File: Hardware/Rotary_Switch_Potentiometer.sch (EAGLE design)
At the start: 16 parts, among them SW1 1x10

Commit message: Small schem update.
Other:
- note added: "Resistor values can be selected for desired response."
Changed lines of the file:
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@@
 <text x="165.1" y="7.62" size="2.54" layer="94" font="vector">Byron Jacquot</text>
 <text x="238.76" y="7.62" size="2.54" layer="94" font="vector">V01</text>
+<text x="99.06" y="66.04" size="1.778" layer="97">Resistor values can be selected for desired response.</text>
 </plain>
 <instances>
@@
 </sheet>
 </sheets>
+<errors>
+</errors>
 </schematic>
 </drawing>

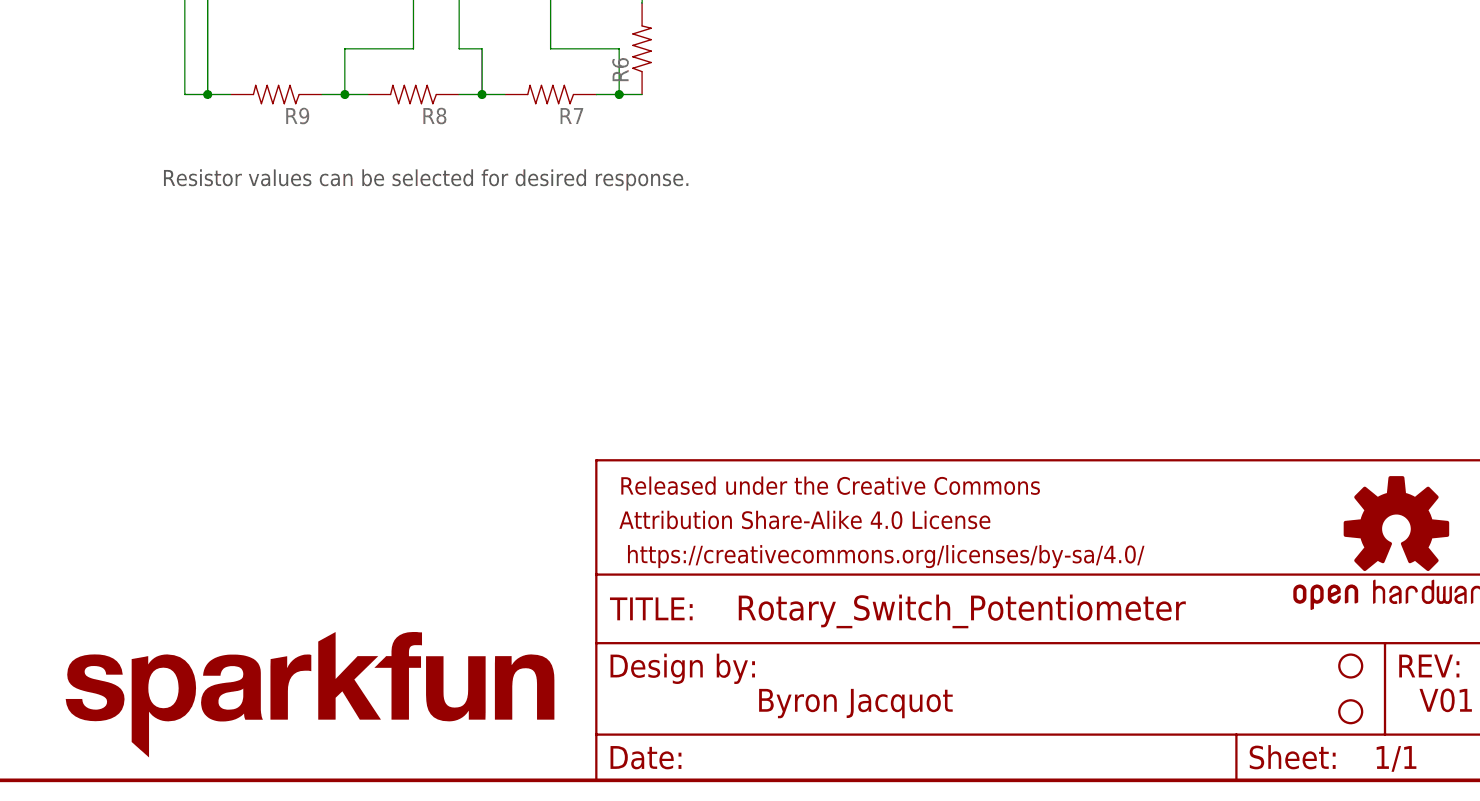
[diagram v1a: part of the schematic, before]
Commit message: Updates from working with protos.
Now has 4 mounting holes.
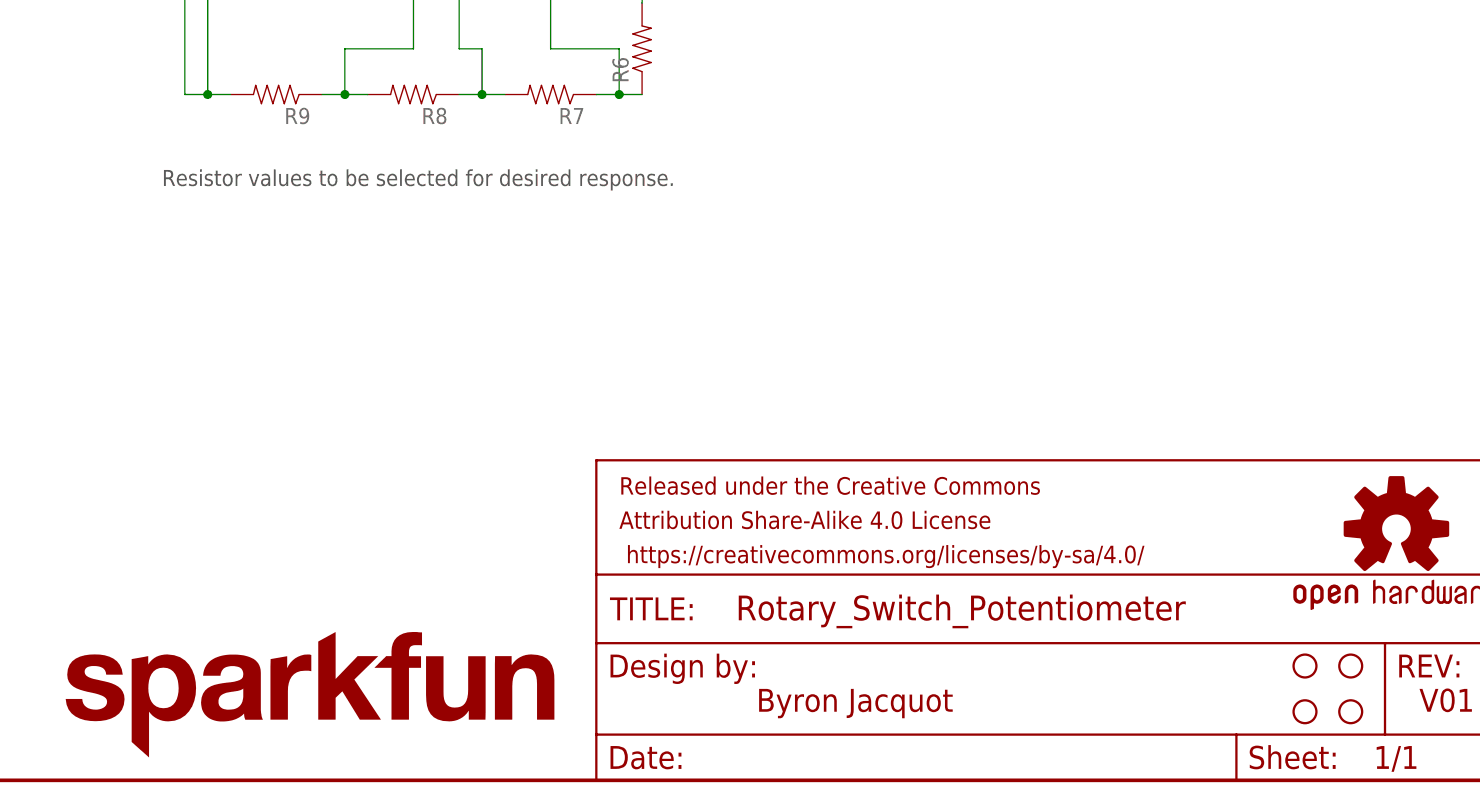
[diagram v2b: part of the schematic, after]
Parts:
- added STANDOFF5, STANDOFF6: STAND-OFF, SparkFun-Electromechanical:STAND-OFF
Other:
- note added: "Resistor values to be selected for desired response."
- note removed: "Resistor values can be selected for desired response."
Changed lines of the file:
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@@
 <?xml version="1.0" encoding="utf-8"?>
 <!DOCTYPE eagle SYSTEM "eagle.dtd">
-<eagle version="6.5.0">
+<eagle version="7.1.0">
 <drawing>
 <settings>
@@
 <part name="R8" library="SparkFun-Resistors" deviceset="RESISTOR" device="PTH-1/4W-VERT-KIT"/>
 <part name="R9" library="SparkFun-Resistors" deviceset="RESISTOR" device="PTH-1/4W-VERT-KIT"/>
+<part name="STANDOFF5" library="SparkFun-Electromechanical" deviceset="STAND-OFF" device=""/>
+<part name="STANDOFF6" library="SparkFun-Electromechanical" deviceset="STAND-OFF" device=""/>
 </parts>
 <sheets>
@@
 <text x="165.1" y="7.62" size="2.54" layer="94" font="vector">Byron Jacquot</text>
 <text x="238.76" y="7.62" size="2.54" layer="94" font="vector">V01</text>
-<text x="99.06" y="66.04" size="1.778" layer="97">Resistor values can be selected for desired response.</text>
+<text x="99.06" y="66.04" size="1.778" layer="97">Resistor values to be selected for desired response.</text>
 </plain>
 <instances>
@@
 <instance part="R8" gate="G$1" x="127" y="76.2" rot="R180"/>
 <instance part="R9" gate="G$1" x="111.76" y="76.2" rot="R180"/>
+<instance part="STANDOFF5" gate="G$1" x="226.06" y="12.7"/>
+<instance part="STANDOFF6" gate="G$1" x="226.06" y="7.62"/>
 </instances>
 <busses>

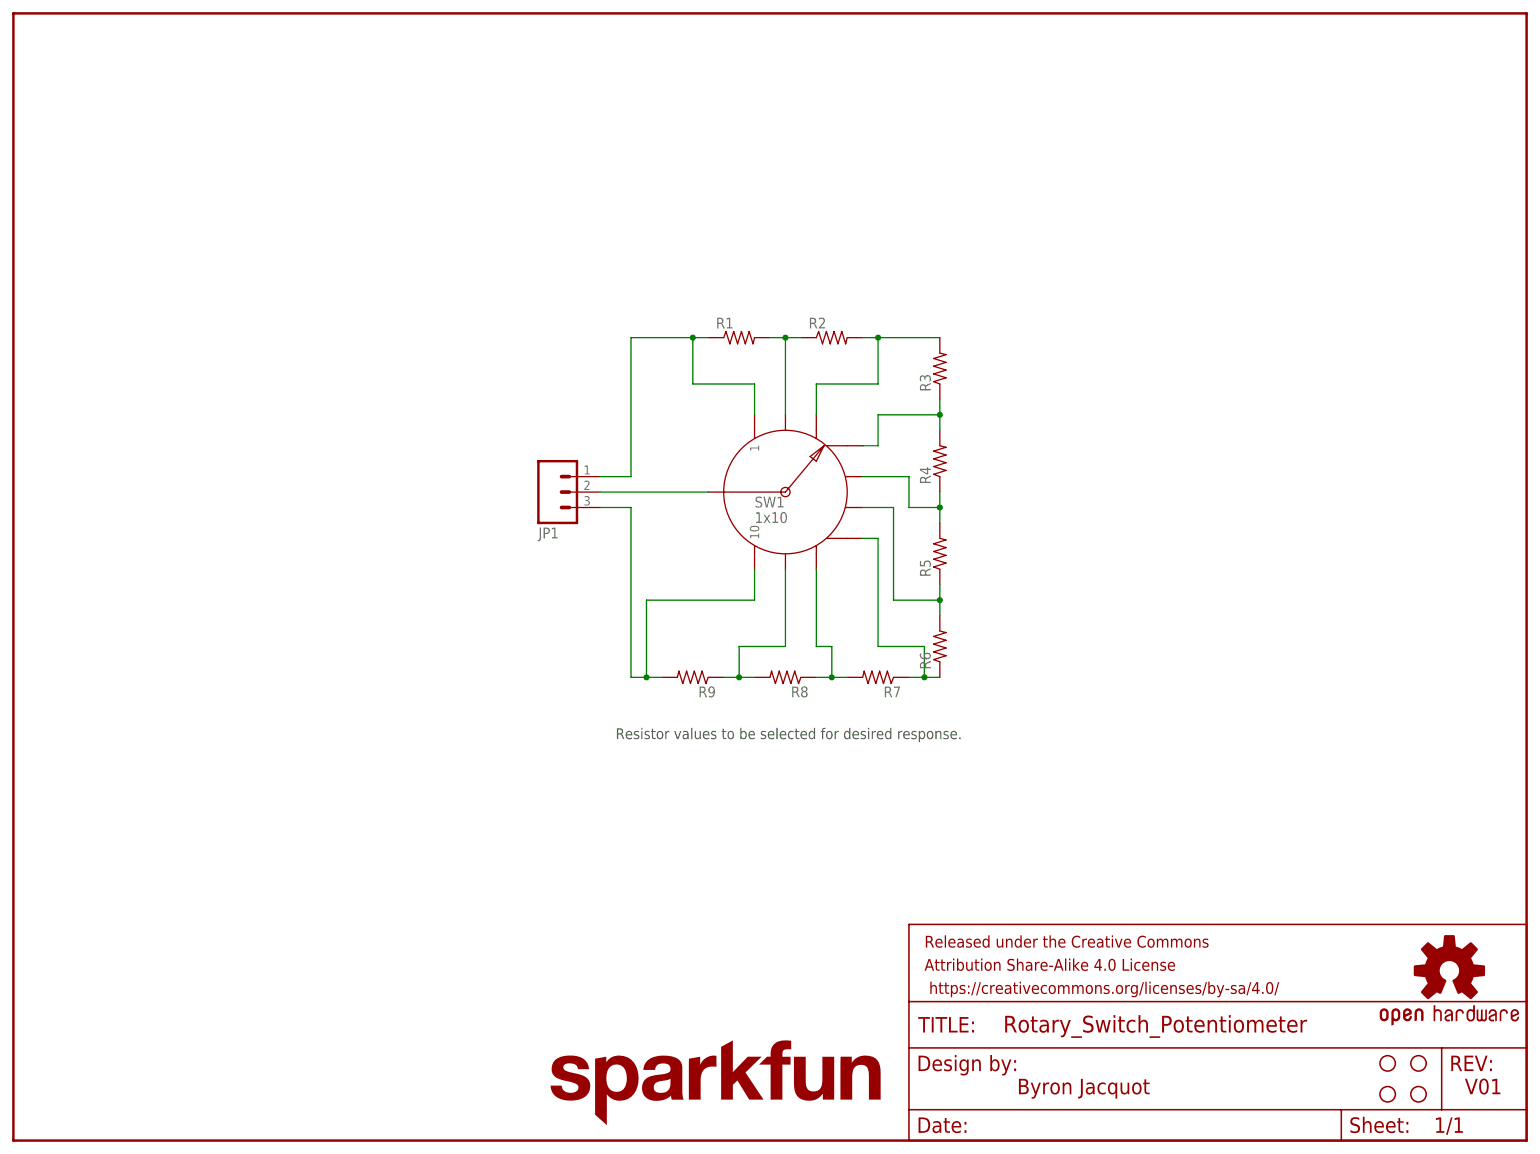
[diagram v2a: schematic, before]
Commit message: Tweaks after engineering group review.
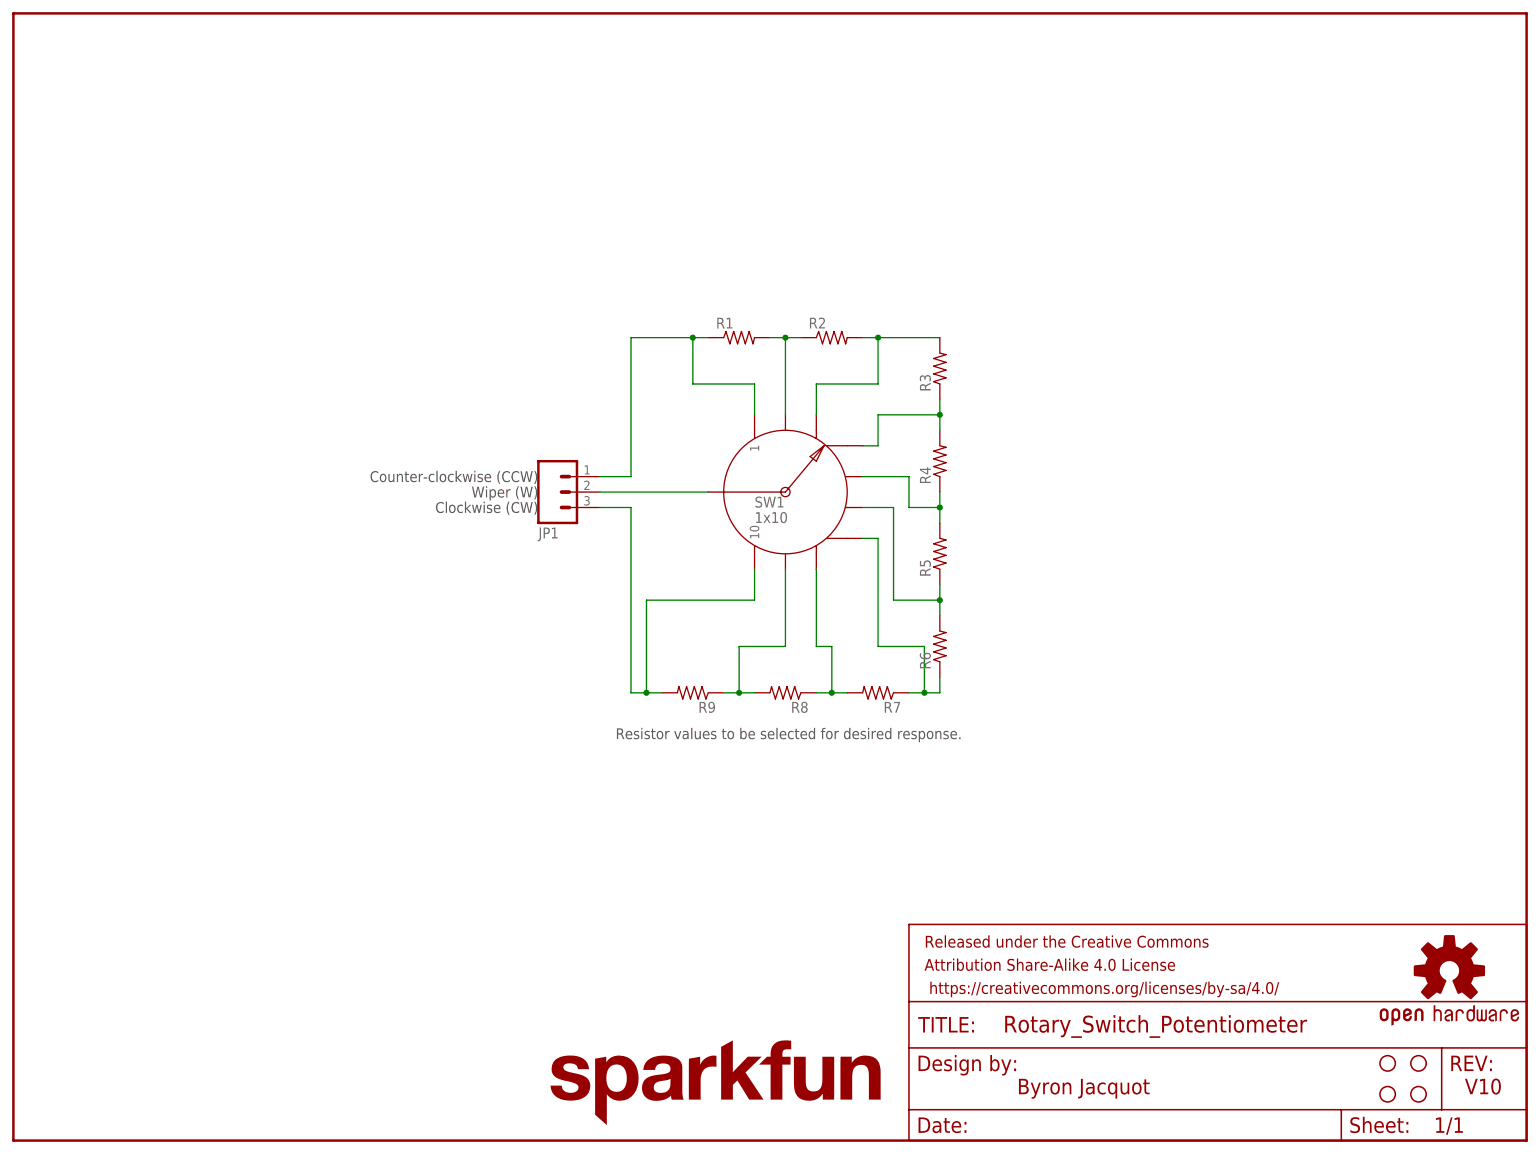
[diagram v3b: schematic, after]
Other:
- note added: "Clockwise (CW)"
- note added: "Counter-clockwise (CCW)"
- note added: "V10"
- note added: "Wiper (W)"
- note removed: "V01"
- moved on the sheet: R7, R8, R9
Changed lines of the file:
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@@
 <plain>
 <text x="165.1" y="7.62" size="2.54" layer="94" font="vector">Byron Jacquot</text>
-<text x="238.76" y="7.62" size="2.54" layer="94" font="vector">V01</text>
+<text x="238.76" y="7.62" size="2.54" layer="94" font="vector">V10</text>
 <text x="99.06" y="66.04" size="1.778" layer="97">Resistor values to be selected for desired response.</text>
+<text x="86.36" y="106.68" size="1.778" layer="97" align="center-right">Wiper (W)</text>
+<text x="86.36" y="109.22" size="1.778" layer="97" align="center-right">Counter-clockwise (CCW)</text>
+<text x="86.36" y="104.14" size="1.778" layer="97" align="center-right">Clockwise (CW)</text>
 </plain>
 <instances>
@@
 <instance part="R5" gate="G$1" x="152.4" y="96.52" rot="R90"/>
 <instance part="R6" gate="G$1" x="152.4" y="81.28" rot="R90"/>
-<instance part="R7" gate="G$1" x="142.24" y="76.2" rot="R180"/>
-<instance part="R8" gate="G$1" x="127" y="76.2" rot="R180"/>
-<instance part="R9" gate="G$1" x="111.76" y="76.2" rot="R180"/>
+<instance part="R7" gate="G$1" x="142.24" y="73.66" rot="R180"/>
+<instance part="R8" gate="G$1" x="127" y="73.66" rot="R180"/>
+<instance part="R9" gate="G$1" x="111.76" y="73.66" rot="R180"/>
 <instance part="STANDOFF5" gate="G$1" x="226.06" y="12.7"/>
 <instance part="STANDOFF6" gate="G$1" x="226.06" y="7.62"/>
@@
 <net name="N$3" class="0">
 <segment>
-<wire x1="101.6" y1="104.14" x2="101.6" y2="76.2" width="0.1524" layer="91"/>
+<wire x1="101.6" y1="104.14" x2="101.6" y2="73.66" width="0.1524" layer="91"/>
 <pinref part="R9" gate="G$1" pin="2"/>
-<wire x1="101.6" y1="76.2" x2="104.14" y2="76.2" width="0.1524" layer="91"/>
+<wire x1="101.6" y1="73.66" x2="104.14" y2="73.66" width="0.1524" layer="91"/>
 <pinref part="SW1" gate="G$1" pin="10"/>
-<wire x1="104.14" y1="76.2" x2="106.68" y2="76.2" width="0.1524" layer="91"/>
+<wire x1="104.14" y1="73.66" x2="106.68" y2="73.66" width="0.1524" layer="91"/>
 <wire x1="121.92" y1="93.98" x2="121.92" y2="88.9" width="0.1524" layer="91"/>
 <wire x1="121.92" y1="88.9" x2="104.14" y2="88.9" width="0.1524" layer="91"/>
-<wire x1="104.14" y1="88.9" x2="104.14" y2="76.2" width="0.1524" layer="91"/>
-<junction x="104.14" y="76.2"/>
+<wire x1="104.14" y1="88.9" x2="104.14" y2="73.66" width="0.1524" layer="91"/>
+<junction x="104.14" y="73.66"/>
 <pinref part="JP1" gate="G$1" pin="3"/>
 <wire x1="96.52" y1="104.14" x2="101.6" y2="104.14" width="0.1524" layer="91"/>
@@
 <pinref part="R6" gate="G$1" pin="1"/>
 <pinref part="R7" gate="G$1" pin="1"/>
-<wire x1="152.4" y1="76.2" x2="149.86" y2="76.2" width="0.1524" layer="91"/>
+<wire x1="152.4" y1="76.2" x2="152.4" y2="73.66" width="0.1524" layer="91"/>
+<wire x1="152.4" y1="73.66" x2="149.86" y2="73.66" width="0.1524" layer="91"/>
 <pinref part="SW1" gate="G$1" pin="7"/>
-<wire x1="149.86" y1="76.2" x2="147.32" y2="76.2" width="0.1524" layer="91"/>
+<wire x1="149.86" y1="73.66" x2="147.32" y2="73.66" width="0.1524" layer="91"/>
 <wire x1="139.7" y1="99.06" x2="142.24" y2="99.06" width="0.1524" layer="91"/>
 <wire x1="142.24" y1="99.06" x2="142.24" y2="81.28" width="0.1524" layer="91"/>
 <wire x1="142.24" y1="81.28" x2="149.86" y2="81.28" width="0.1524" layer="91"/>
-<wire x1="149.86" y1="81.28" x2="149.86" y2="76.2" width="0.1524" layer="91"/>
-<junction x="149.86" y="76.2"/>
+<wire x1="149.86" y1="81.28" x2="149.86" y2="73.66" width="0.1524" layer="91"/>
+<junction x="149.86" y="73.66"/>
 </segment>
 </net>
@@
 <pinref part="R8" gate="G$1" pin="2"/>
 <pinref part="R9" gate="G$1" pin="1"/>
-<wire x1="121.92" y1="76.2" x2="119.38" y2="76.2" width="0.1524" layer="91"/>
-<wire x1="119.38" y1="76.2" x2="116.84" y2="76.2" width="0.1524" layer="91"/>
-<wire x1="119.38" y1="81.28" x2="119.38" y2="76.2" width="0.1524" layer="91"/>
-<junction x="119.38" y="76.2"/>
+<wire x1="121.92" y1="73.66" x2="119.38" y2="73.66" width="0.1524" layer="91"/>
+<wire x1="119.38" y1="73.66" x2="116.84" y2="73.66" width="0.1524" layer="91"/>
+<wire x1="119.38" y1="81.28" x2="119.38" y2="73.66" width="0.1524" layer="91"/>
+<junction x="119.38" y="73.66"/>
 </segment>
 </net>
@@
 <pinref part="R8" gate="G$1" pin="1"/>
 <pinref part="R7" gate="G$1" pin="2"/>
-<wire x1="137.16" y1="76.2" x2="134.62" y2="76.2" width="0.1524" layer="91"/>
-<wire x1="134.62" y1="81.28" x2="134.62" y2="76.2" width="0.1524" layer="91"/>
-<junction x="134.62" y="76.2"/>
-<wire x1="134.62" y1="76.2" x2="132.08" y2="76.2" width="0.1524" layer="91"/>
+<wire x1="137.16" y1="73.66" x2="134.62" y2="73.66" width="0.1524" layer="91"/>
+<wire x1="134.62" y1="81.28" x2="134.62" y2="73.66" width="0.1524" layer="91"/>
+<junction x="134.62" y="73.66"/>
+<wire x1="134.62" y1="73.66" x2="132.08" y2="73.66" width="0.1524" layer="91"/>
 <wire x1="134.62" y1="81.28" x2="132.08" y2="81.28" width="0.1524" layer="91"/>
 <pinref part="SW1" gate="G$1" pin="8"/>
